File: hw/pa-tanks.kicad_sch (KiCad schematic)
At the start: 84 parts, among them IC2201 TPL7407LADR, K2201 G2RL-1A, K2202 G2RL-1A, K2203 G2RL-1A, Q2201 2N7002, Q2202 2N7002, Q2203 2N7002, Q2204 2N7002, Q2205 2N7002, Q2206 2N7002, Q2207 2N7002, Q2208 2N7002, Q2209 2N7002, Q2210 2N7002

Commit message: Embarking on a whole new arch for rx without BPFs and using a single digitally tuned tank plus three QSDs to accomplish image rejection in digital domain
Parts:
- C2001: renamed from C2201; footprint (none) -> Capacitor_SMD:C_1206_3216Metric
- C2002: renamed from C2202; footprint (none) -> Capacitor_SMD:C_1206_3216Metric
- C2003: renamed from C2203; footprint (none) -> Capacitor_SMD:C_1206_3216Metric
- C2004: renamed from C2206; footprint (none) -> Capacitor_SMD:C_1206_3216Metric
- C2005: renamed from C2207; footprint (none) -> Capacitor_SMD:C_1206_3216Metric
- C2006: renamed from C2208; footprint (none) -> Capacitor_SMD:C_1206_3216Metric
- C2007: renamed from C2204; footprint (none) -> Capacitor_SMD:C_0805_2012Metric
- C2008: renamed from C2205; footprint (none) -> Capacitor_SMD:C_0805_2012Metric
- C2009: renamed from C2209; footprint (none) -> Capacitor_SMD:C_1206_3216Metric
- C2010: renamed from C2210; footprint (none) -> Capacitor_SMD:C_1206_3216Metric
- C2011: renamed from C2211; footprint (none) -> Capacitor_SMD:C_1206_3216Metric
- C2012: renamed from C2212; footprint (none) -> Capacitor_SMD:C_1206_3216Metric
- C2013: renamed from C2213; footprint (none) -> Capacitor_SMD:C_1206_3216Metric
- C2014: renamed from C2214; footprint (none) -> Capacitor_SMD:C_1206_3216Metric
- C2015: renamed from C2215; footprint (none) -> Capacitor_SMD:C_1206_3216Metric
- C2016: renamed from C2216; footprint (none) -> Capacitor_SMD:C_1206_3216Metric
- C2017: renamed from C2217; footprint (none) -> Capacitor_SMD:C_1206_3216Metric
- C2018: renamed from C2218; footprint (none) -> Capacitor_SMD:C_1206_3216Metric
- C2019: renamed from C2221; footprint (none) -> Capacitor_SMD:C_1206_3216Metric
- C2020: renamed from C2224; footprint (none) -> Capacitor_SMD:C_1206_3216Metric
- C2021: renamed from C2219; footprint (none) -> Capacitor_SMD:C_1206_3216Metric
- C2022: renamed from C2220; footprint (none) -> Capacitor_SMD:C_1206_3216Metric
- C2023: renamed from C2225; footprint (none) -> Capacitor_SMD:C_1206_3216Metric
- C2024: renamed from C2222; footprint (none) -> Capacitor_SMD:C_1206_3216Metric
- C2025: renamed from C2223; footprint (none) -> Capacitor_SMD:C_1206_3216Metric
- D2001: renamed from D2201; footprint SODFL1608X70N -> Library:SC-79
- D2002: renamed from D2202; footprint SODFL1608X70N -> Library:SC-79
- D2003: renamed from D2203; footprint SODFL1608X70N -> Library:SC-79
- D2004: renamed from D2204; footprint SODFL1608X70N -> Library:SC-79
- D2005: renamed from D2205; footprint SODFL1608X70N -> Library:SC-79
- D2006: renamed from D2207; footprint SODFL1608X70N -> Library:SC-79
- D2007: renamed from D2206; footprint SODFL1608X70N -> Library:SC-79
- D2008: renamed from D2209; footprint SODFL1608X70N -> Library:SC-79
- D2009: renamed from D2210; footprint SODFL1608X70N -> Library:SC-79
- D2010: renamed from D2208; footprint SODFL1608X70N -> Library:SC-79
- IC2001: renamed from IC2201; footprint SOIC127P600X175-16N -> Package_SO:JEITA_SOIC-16_3.9x9.9mm_P1.27mm
- L2001: renamed from L2201; footprint (none) -> Inductor_SMD:L_0805_2012Metric
- L2002: renamed from L2202; footprint (none) -> Inductor_SMD:L_0805_2012Metric
- L2003: renamed from L2203; footprint (none) -> Inductor_SMD:L_0805_2012Metric
- L2004: renamed from L2204; footprint (none) -> Inductor_SMD:L_0805_2012Metric
- L2005: renamed from L2206; footprint (none) -> Inductor_SMD:L_0805_2012Metric
- L2007: renamed from L2208; footprint (none) -> Inductor_SMD:L_0805_2012Metric
- L2009: renamed from L2210; footprint (none) -> Inductor_SMD:L_0805_2012Metric
- L2011: renamed from L2212; footprint (none) -> Inductor_SMD:L_0805_2012Metric
- L2012: renamed from L2211; footprint (none) -> Inductor_SMD:L_0805_2012Metric
- L2013: renamed from L2214; footprint (none) -> Inductor_SMD:L_0805_2012Metric
- L2014: renamed from L2215; footprint (none) -> Inductor_SMD:L_0805_2012Metric
- L2015: renamed from L2213; footprint (none) -> Inductor_SMD:L_0805_2012Metric
- R2001: renamed from R2201; footprint (none) -> Capacitor_SMD:C_1206_3216Metric
- R2002: renamed from R2202; footprint (none) -> Capacitor_SMD:C_1206_3216Metric
- R2003: renamed from R2203; footprint (none) -> Capacitor_SMD:C_1206_3216Metric
- R2004: renamed from R2204; footprint (none) -> Capacitor_SMD:C_1206_3216Metric
- R2005: renamed from R2205; footprint (none) -> Capacitor_SMD:C_1206_3216Metric
- R2006: renamed from R2206; footprint (none) -> Capacitor_SMD:C_1206_3216Metric
- R2007: renamed from R2207; footprint (none) -> Capacitor_SMD:C_1206_3216Metric
- R2008: renamed from R2208; footprint (none) -> Capacitor_SMD:C_1206_3216Metric
- R2009: renamed from R2209; footprint (none) -> Capacitor_SMD:C_1206_3216Metric
- R2010: renamed from R2211; footprint (none) -> Capacitor_SMD:C_1206_3216Metric
- R2011: renamed from R2213; footprint (none) -> Capacitor_SMD:C_1206_3216Metric
- R2012: renamed from R2214; footprint (none) -> Capacitor_SMD:C_1206_3216Metric
- R2013: renamed from R2210; footprint (none) -> Capacitor_SMD:C_1206_3216Metric
- R2014: renamed from R2217; footprint (none) -> Capacitor_SMD:C_1206_3216Metric
- R2015: renamed from R2212; footprint (none) -> Capacitor_SMD:C_1206_3216Metric
- R2016: renamed from R2218; footprint (none) -> Capacitor_SMD:C_1206_3216Metric
- R2017: renamed from R2219; footprint (none) -> Capacitor_SMD:C_1206_3216Metric
- R2018: renamed from R2220; footprint (none) -> Capacitor_SMD:C_1206_3216Metric
- R2019: renamed from R2215; footprint (none) -> Capacitor_SMD:C_1206_3216Metric
- R2020: renamed from R2216; footprint (none) -> Capacitor_SMD:C_1206_3216Metric
- renumbered K2201 to K2001, K2202 to K2002, K2203 to K2003, L2205 to L2006, L2207 to L2008, L2209 to L2010, Q2201 to Q2001, Q2202 to Q2002, Q2203 to Q2003, Q2204 to Q2004, Q2205 to Q2005, Q2207 to Q2006, Q2206 to Q2007, Q2209 to Q2008, Q2210 to Q2009, Q2208 to Q2010
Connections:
- net PAtankSel.C0: now also Q2009.1 (G)
- net PAtankSel.C1: now also Q2008.1 (G)
- net PAtankSel.C2: now also Q2006.1 (G)
- net PAtankSel.C3: now also Q2005.1 (G)
- net PAtankSel.C5: now also Q2003.1 (G)
- net PAtankSel.C6: now also Q2002.1 (G)
- net PAtankSel.C7: now also Q2001.1 (G)
- net PAL1 renamed PAtankSel.L1
- net PAL2 renamed PAtankSel.L2
- net PAL3 renamed PAtankSel.L3
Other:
- title: (none) -> PA Tanks
- moved on the sheet: C2001, C2002, C2003, C2004, C2005, C2006, C2009, C2010, C2011, C2012, C2013, C2014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

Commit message: Starting to switch to new rx architecture
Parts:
- renumbered C2001 to C2201, C2002 to C2202, C2003 to C2203, C2004 to C2204, C2005 to C2205, C2006 to C2206, C2007 to C2207, C2008 to C2208, C2009 to C2209, C2010 to C2210, C2011 to C2211, C2012 to C2212, C2013 to C2213, C2014 to C2214, C2015 to C2215, C2016 to C2216, C2017 to C2217, C2018 to C2218, C2019 to C2219, C2020 to C2220, C2021 to C2221, C2022 to C2222, C2023 to C2223, C2024 to C2224, C2025 to C2225, D2001 to D2201, D2002 to D2202, D2003 to D2203, D2004 to D2204, D2005 to D2205, D2006 to D2206, D2007 to D2207, D2008 to D2208, D2009 to D2209, D2010 to D2210, IC2001 to IC2201, K2001 to K2201, K2002 to K2202, K2003 to K2203, L2001 to L2201, L2002 to L2202, L2003 to L2203, L2004 to L2204, L2005 to L2205, L2006 to L2206, L2007 to L2207, L2008 to L2208, L2009 to L2209, L2010 to L2210, L2011 to L2211, L2012 to L2212, L2013 to L2213, L2014 to L2214, L2015 to L2215, Q2001 to Q2201, Q2002 to Q2202, Q2003 to Q2203, Q2004 to Q2204, Q2005 to Q2205, Q2006 to Q2206, Q2007 to Q2207, Q2008 to Q2208, Q2009 to Q2209, Q2010 to Q2210, R2001 to R2201, R2002 to R2202, R2003 to R2203, R2004 to R2204, R2005 to R2205, R2006 to R2206, R2007 to R2207, R2008 to R2208, R2009 to R2209, R2010 to R2210, R2011 to R2211, R2012 to R2212, R2013 to R2213, R2014 to R2214, R2015 to R2215, R2016 to R2216, R2017 to R2217, R2018 to R2218, R2019 to R2219, R2020 to R2220

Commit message: Converting to use busses as global symbols instead of tedium. Using 2n7002 Nexperia dual MOSFET because of its LOW LOW capacitance spec for L, C, and attenuator switching.
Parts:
- removed Q2201, Q2202, Q2203, Q2204, Q2205, Q2206, Q2207, Q2208, Q2209, Q2210: 2N7002, Package_TO_SOT_SMD:SOT-23, symbol Transistor_FET:2N7002
- added Q2001, Q2002, Q2003, Q2004, Q2005: 2N7002AKRA-QZ, 2N7002AKRAQZ, symbol 2N7002AKRA-QZ:2N7002AKRA-QZ
- renumbered C2201 to C2001, C2202 to C2002, C2203 to C2003, C2204 to C2004, C2205 to C2005, C2206 to C2006, C2207 to C2007, C2208 to C2008, C2209 to C2009, C2210 to C2010, C2211 to C2011, C2212 to C2012, C2213 to C2013, C2214 to C2014, C2215 to C2015, C2216 to C2016, C2217 to C2017, C2218 to C2018, C2219 to C2019, C2220 to C2020, C2221 to C2021, C2222 to C2022, C2223 to C2023, C2224 to C2024, C2225 to C2025, D2201 to D2001, D2202 to D2002, D2203 to D2003, D2204 to D2004, D2205 to D2005, D2206 to D2006, D2207 to D2007, D2208 to D2008, D2209 to D2009, D2210 to D2010, IC2201 to IC2001, K2201 to K2001, K2202 to K2002, K2203 to K2003, L2201 to L2001, L2202 to L2002, L2203 to L2003, L2204 to L2004, L2205 to L2005, L2206 to L2006, L2207 to L2007, L2208 to L2008, L2209 to L2009, L2210 to L2010, L2211 to L2011, L2212 to L2012, L2213 to L2013, L2214 to L2014, L2215 to L2015, R2201 to R2001, R2202 to R2002, R2203 to R2003, R2204 to R2004, R2205 to R2005, R2206 to R2006, R2207 to R2007, R2208 to R2008, R2209 to R2009, R2210 to R2010, R2211 to R2011, R2212 to R2012, R2213 to R2013, R2214 to R2014, R2215 to R2015, R2216 to R2016, R2217 to R2017, R2218 to R2018, R2219 to R2019, R2220 to R2020
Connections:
- net GND: now also Q2001.1 (S1), Q2001.4 (S2), Q2002.1 (S1), Q2002.4 (S2), Q2003.1 (S1), Q2003.4 (S2), Q2004.1 (S1), Q2004.4 (S2), Q2005.1 (S1), Q2005.4 (S2)
- net PA160m: now also Q2005.2 (G1)
- net PA80m: now also Q2005.5 (G2)
- net PAtankSel.C0: now also Q2004.5 (G2)
- net PAtankSel.C1: now also Q2004.2 (G1)
- net PAtankSel.C2: now also Q2003.5 (G2)
- net PAtankSel.C3: now also Q2003.2 (G1)
- net PAtankSel.C5: now also Q2002.2 (G1)
- net PAtankSel.C6: now also Q2001.5 (G2)
- net PAtankSel.C7: now also Q2001.2 (G1)
- net at R2016.2: now also Q2004.6 (D1), Q2004.7 (D2)
- net at R2010.2: now also Q2003.6 (D1), Q2003.7 (D2)
- net at R2008.2: now also Q2002.3 (D2_1), Q2002.8 (D2_2)
- net at R2018.2: now also Q2004.3 (D2_1), Q2004.8 (D2_2)
- net at R2015.2: now also Q2005.6 (D1), Q2005.7 (D2)
- net at R2002.2: now also Q2001.6 (D1), Q2001.7 (D2)
- net at R2006.2: now also Q2002.6 (D1), Q2002.7 (D2)
- net at R2020.2: now also Q2005.3 (D2_1), Q2005.8 (D2_2)
- net at R2004.2: now also Q2001.3 (D2_1), Q2001.8 (D2_2)
- net at R2012.2: now also Q2003.3 (D2_1), Q2003.8 (D2_2)

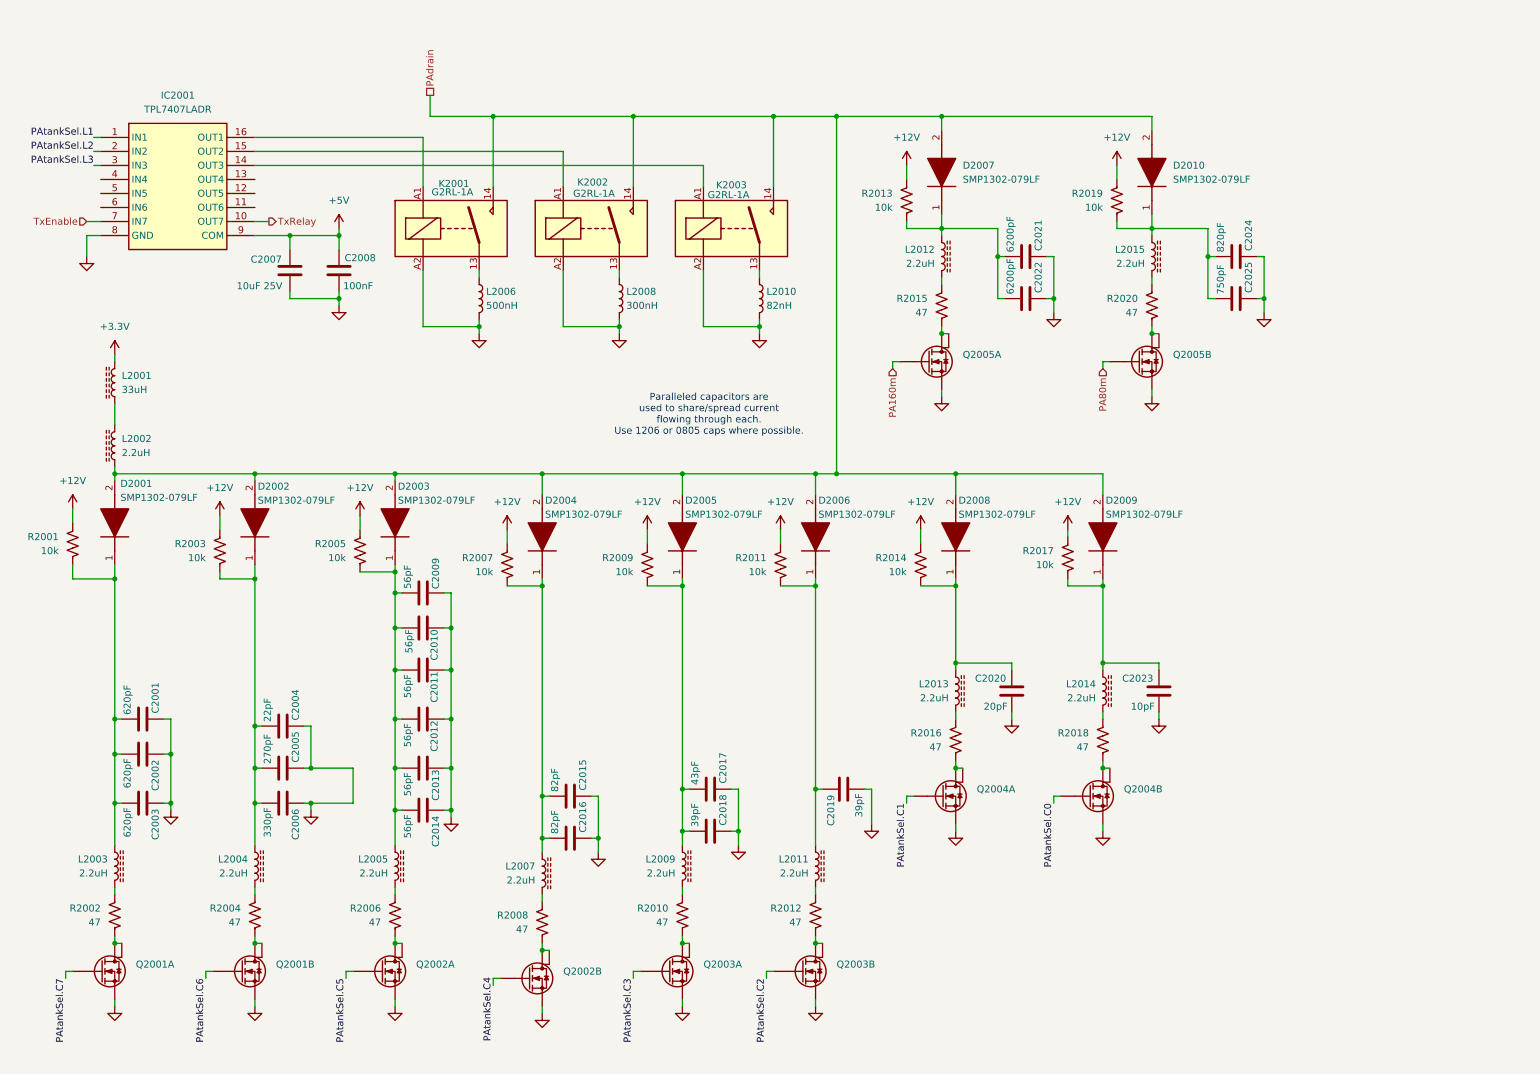
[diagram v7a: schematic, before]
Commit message: LC tank for tx side is now switch C + switch L using reed relays. Rx preselector in flux but coming together
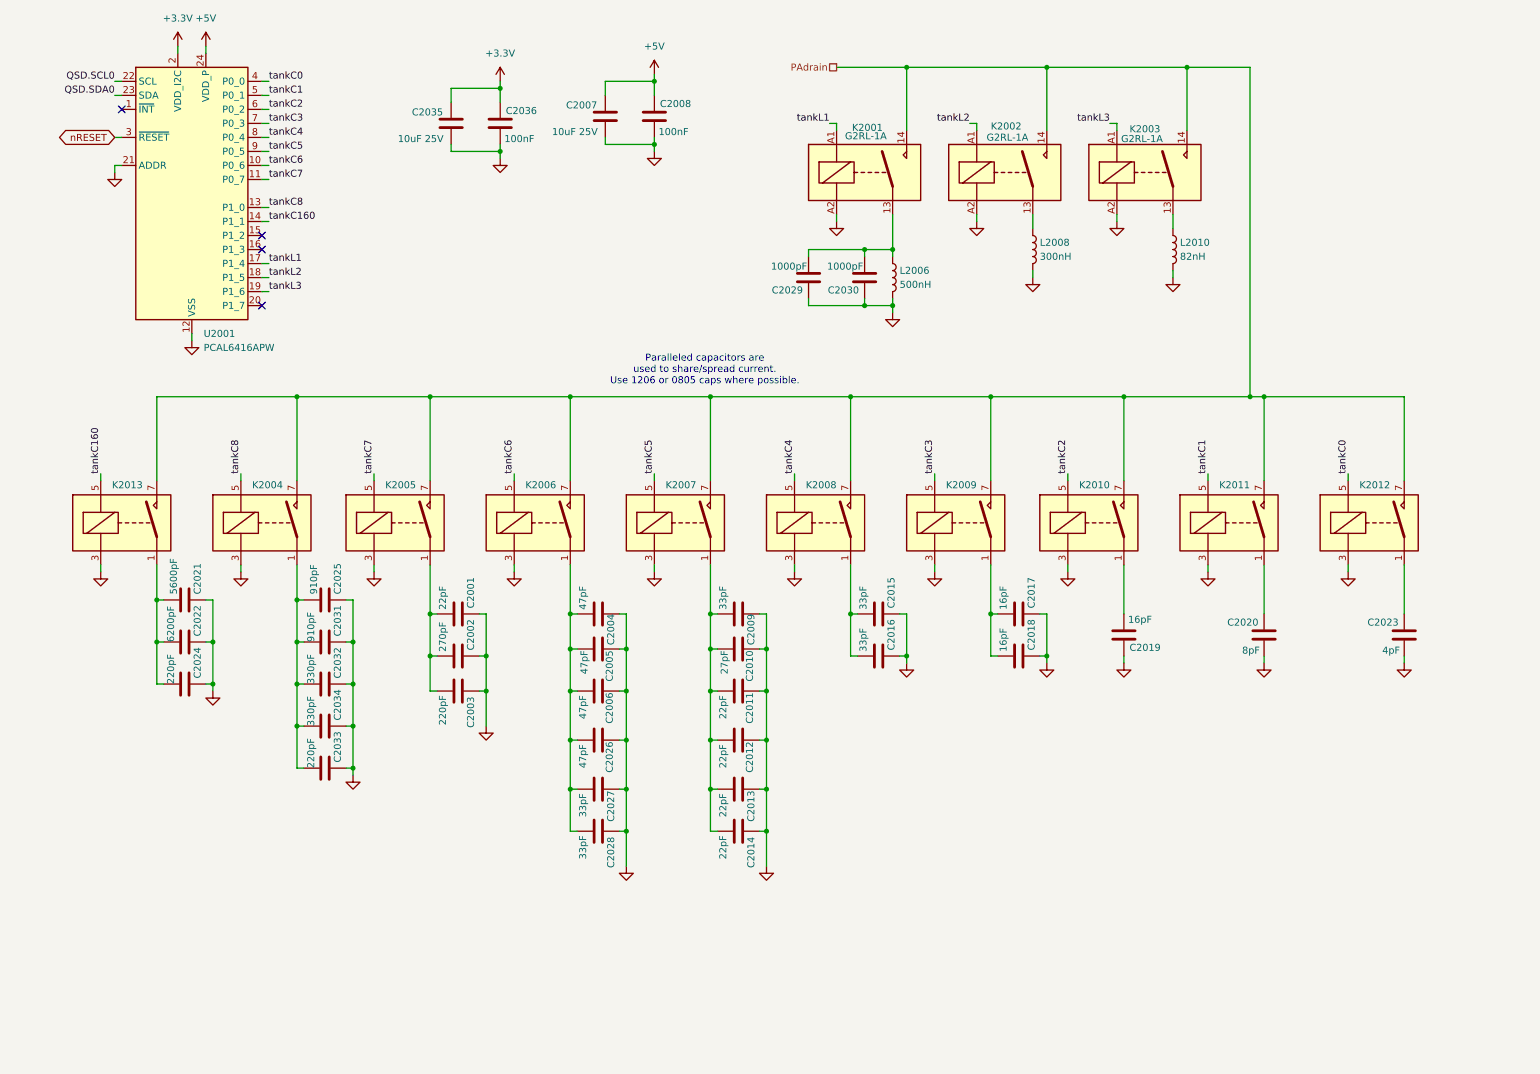
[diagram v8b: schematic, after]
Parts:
- removed D2001, D2002, D2003, D2004, D2005, D2006, D2007, D2008, D2009, D2010: SMP1302-079LF, Library:SC-79, symbol SMP1302-079LF:SMP1302-079LF
- removed IC2001: TPL7407LADR, Package_SO:JEITA_SOIC-16_3.9x9.9mm_P1.27mm, symbol TPL7407LADR:TPL7407LADR
- removed L2001: 33uH, Inductor_SMD:L_0805_2012Metric, symbol Device:L_Ferrite
- removed L2002, L2003, L2004, L2005, L2007, L2009, L2011, L2012, L2013, L2014, L2015: 2.2uH, Inductor_SMD:L_0805_2012Metric, symbol Device:L_Ferrite
- removed Q2001, Q2002, Q2003, Q2004, Q2005: 2N7002AKRA-QZ, 2N7002AKRAQZ, symbol 2N7002AKRA-QZ:2N7002AKRA-QZ
- removed R2001, R2003, R2005, R2007, R2009, R2011, R2013, R2014, R2017, R2019: 10k, Capacitor_SMD:C_1206_3216Metric, symbol Device:R_US
- removed R2002, R2004, R2006, R2008, R2010, R2012, R2015, R2016, R2018, R2020: 47, Capacitor_SMD:C_1206_3216Metric, symbol Device:R_US
- added C2026: 47pF, Capacitor_SMD:C_1206_3216Metric, symbol Device:C
- added C2027, C2028: 33pF, Capacitor_SMD:C_1206_3216Metric, symbol Device:C
- added C2029, C2030: 1000pF, Capacitor_SMD:C_1206_3216Metric, symbol Device:C
- added C2031: 910pF, Capacitor_SMD:C_1206_3216Metric, symbol Device:C
- added C2032, C2034: 330pF, Capacitor_SMD:C_1206_3216Metric, symbol Device:C
- added C2033: 220pF, Capacitor_SMD:C_1206_3216Metric, symbol Device:C
- added C2035: 10uF 25V, Capacitor_SMD:C_0805_2012Metric, symbol Device:C
- added C2036: 100nF, Capacitor_SMD:C_0805_2012Metric, symbol Device:C
- added K2004, K2005, K2006, K2007, K2008, K2009, K2010, K2011, K2012, K2013: SIL05-1A72-71D, Relay_THT:Relay_SPST_StandexMeder_SIL_Form1A, symbol Relay:SILxx-1Axx-71x
- added U2001: PCAL6416APW, Package_SO:TSSOP-24_4.4x7.8mm_P0.65mm, symbol Interface_Expansion:PCAL6416APW
- C2001: value 620pF -> 22pF
- C2002: value 620pF -> 270pF
- C2003: value 620pF -> 220pF
- C2004: value 22pF -> 47pF
- C2005: value 270pF -> 47pF
- C2006: value 330pF -> 47pF
- C2009: value 56pF -> 33pF
- C2010: value 56pF -> 27pF
- C2011, C2012, C2013, C2014: value 56pF -> 22pF
- C2015, C2016: value 82pF -> 33pF
- C2017: value 43pF -> 16pF
- C2018, C2019: value 39pF -> 16pF
- C2020: value 20pF -> 8pF
- C2021: value 6200pF -> 5600pF
- C2023: value 10pF -> 4pF
- C2024: value 820pF -> 220pF
- C2025: value 750pF -> 910pF
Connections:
- net +3.3V: now also C2035.2, C2036.2, U2001.2 (VDD_I2C)
- net +5V: now also U2001.24 (VDD_P)
- net GND: now also C2019.2, C2026.2, C2027.2, C2028.2, C2029.2, C2030.2, C2031.2, C2032.2, C2033.2, C2034.2, C2035.1, C2036.1, K2004.3, K2005.3, K2006.3, K2007.3, K2008.3, K2009.3, K2010.3, K2011.3, K2012.3, K2013.3, U2001.12 (VSS), U2001.21 (ADDR); no longer C2019.1
- net PAdrain: now also K2004.7, K2005.7, K2006.7, K2007.7, K2008.7, K2009.7, K2010.7, K2011.7, K2012.7, K2013.7
- net at C2004.1, C2005.1, C2006.1: now also C2026.1, C2027.1, C2028.1, K2006.1
- net at C2024.1: now also C2021.1, C2022.1, K2013.1; no longer C2025.1
- net at C2020.2: now also K2011.1
- net at K2001.13, L2006.1: now also C2029.1, C2030.1
- net tankL1: now reaches K2001.A1
- net tankL1: now also U2001.17 (P1_4)
- net at C2009.1, C2010.1, C2011.1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: now also K2007.1
- net at C2001.1, C2002.1, C2003.1: now also K2005.1
- net at C2015.1, C2016.1: now also K2008.1
- net at C2017.1, C2018.1: now also K2009.1
- net tankL3: now reaches K2003.A1
- net tankL3: now also U2001.19 (P1_6)
- net at C2023.2: now also K2012.1
- net tankL2: now reaches K2002.A1
- net tankL2: now also U2001.18 (P1_5)
- new net: C2025.1, C2031.1, C2032.1, C2033.1, C2034.1, K2004.1
- new net: C2019.1, K2010.1
- new net QSD.SCL0: U2001.22 (SCL)
- new net QSD.SDA0: U2001.23 (SDA)
- new net nRESET: U2001.3 (~{RESET})
- new net tankC0: K2012.5, U2001.4 (P0_0)
- new net tankC1: K2011.5, U2001.5 (P0_1)
- new net tankC160: K2013.5, U2001.14 (P1_1)
- new net tankC2: K2010.5, U2001.6 (P0_2)
- new net tankC3: K2009.5, U2001.7 (P0_3)
- new net tankC4: K2008.5, U2001.8 (P0_4)
- new net tankC5: K2007.5, U2001.9 (P0_5)
- new net tankC6: K2006.5, U2001.10 (P0_6)
- new net tankC7: K2005.5, U2001.11 (P0_7)
- new net tankC8: K2004.5, U2001.13 (P1_0)
- no-connect marks 0 -> 4
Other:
- note added: "Paralleled capacitors are used to share/spread current. Use 1206 or 0805 caps where possible."
- note removed: "Paralleled capacitors are used to share/spread current flowing through each. Use 1206 or 0805 caps where possible."
- moved on the sheet: C2007, C2008, C2009, C2010, C2011, C2012, C2013, C2014, C2015, C2016, C2017, C2018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
